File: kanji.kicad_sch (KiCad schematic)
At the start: 35 parts, among them J3 E-Ink, Q1 AO3400A, U1 BH1750FVI-TR, U3 SHT4x, U4 XIAO-ESP32-S3-SMD

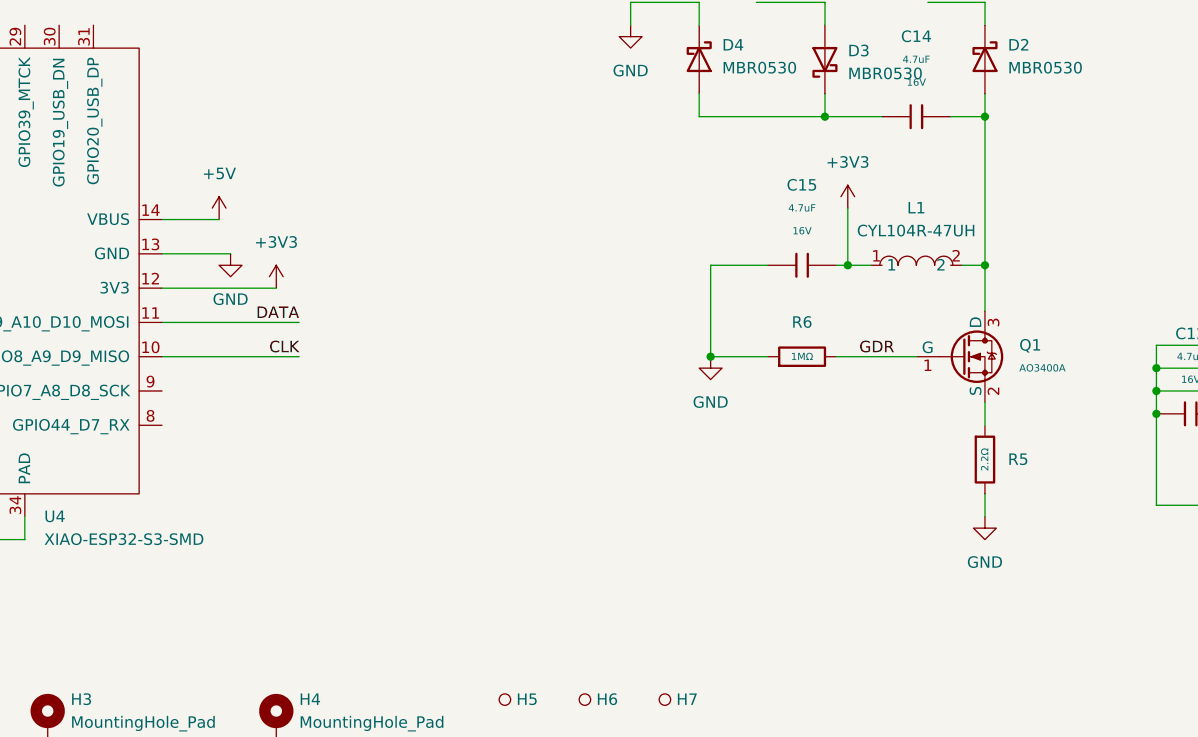
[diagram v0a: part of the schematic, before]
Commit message: feat: add case and update readme
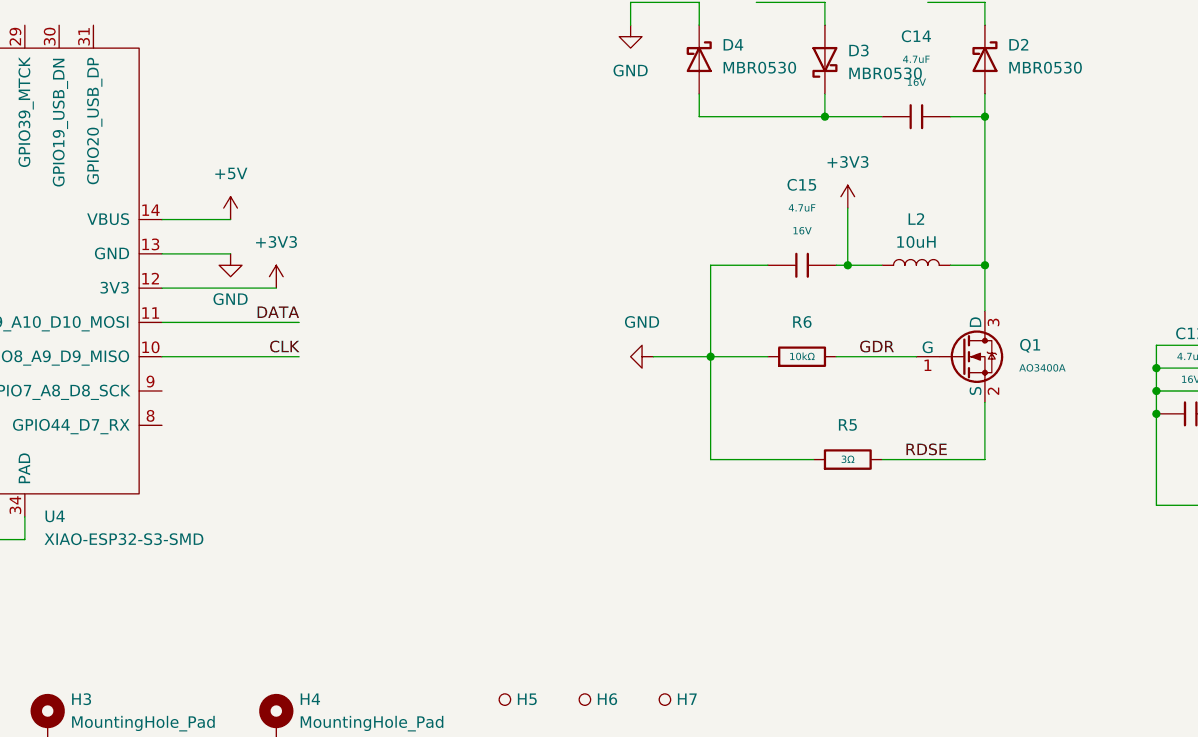
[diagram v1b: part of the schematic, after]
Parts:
- removed L1: CYL104R-47UH, easyeda2kicad:IND-SMD_L10.5-W10.5, symbol easyeda2kicad:CYL104R-47UH
- added L2: 10uH, Inductor_SMD:L_1008_2520Metric, symbol Device:L
- R5: value 2.2Ω -> 3Ω; LCSC C22939 -> C23157
- R6: value 1MΩ -> 10kΩ; symbol PCM_JLCPCB-Resistors:0603,1MΩ -> PCM_JLCPCB-Resistors:0603,10kΩ; LCSC C22935 -> C25804; Part 0603WAF1004T5E -> 0603WAF1002T5E; Resistance 1MΩ -> 10kΩ; Stock 3961571 -> 51181774
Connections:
- net +3V3: now also L2.1
- net GND: now also R5.1; no longer R5.2
- net RDSE: now also Q1.2 (S), R5.2
- net at C14.2, D2.2 (A), Q1.3 (D): now also L2.2
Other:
- moved on the sheet: R5
